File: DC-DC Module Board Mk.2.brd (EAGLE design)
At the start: 177.9 x 101.7 mm, 148 parts, among them U1 PCA9685, U3 LM1085IS-5.0

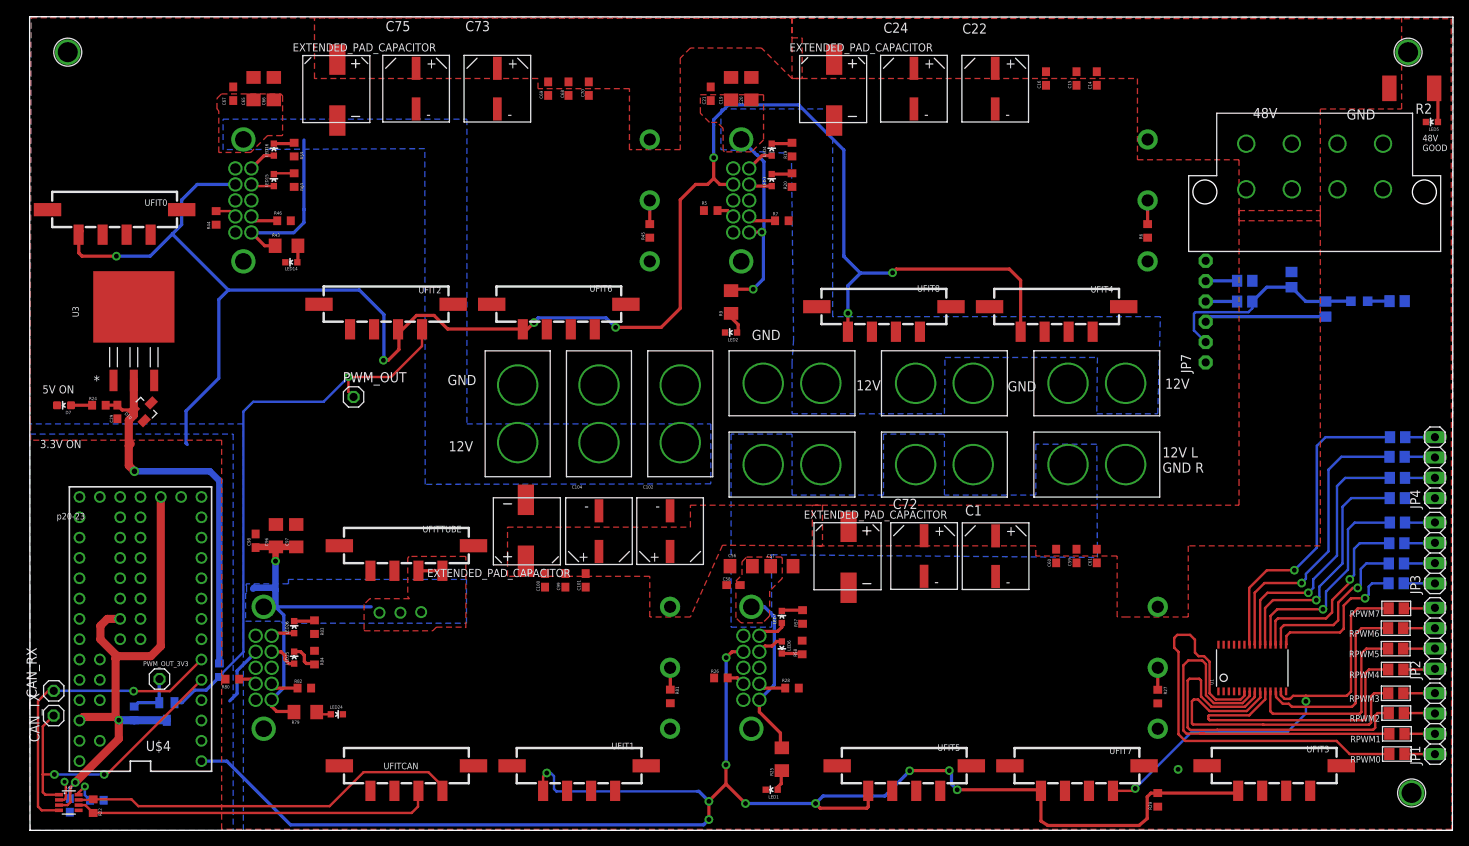
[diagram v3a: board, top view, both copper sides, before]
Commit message: Added and Reworked Traces
Added Traces mostly to the PWN and rerouted and cleaned up some other
traces
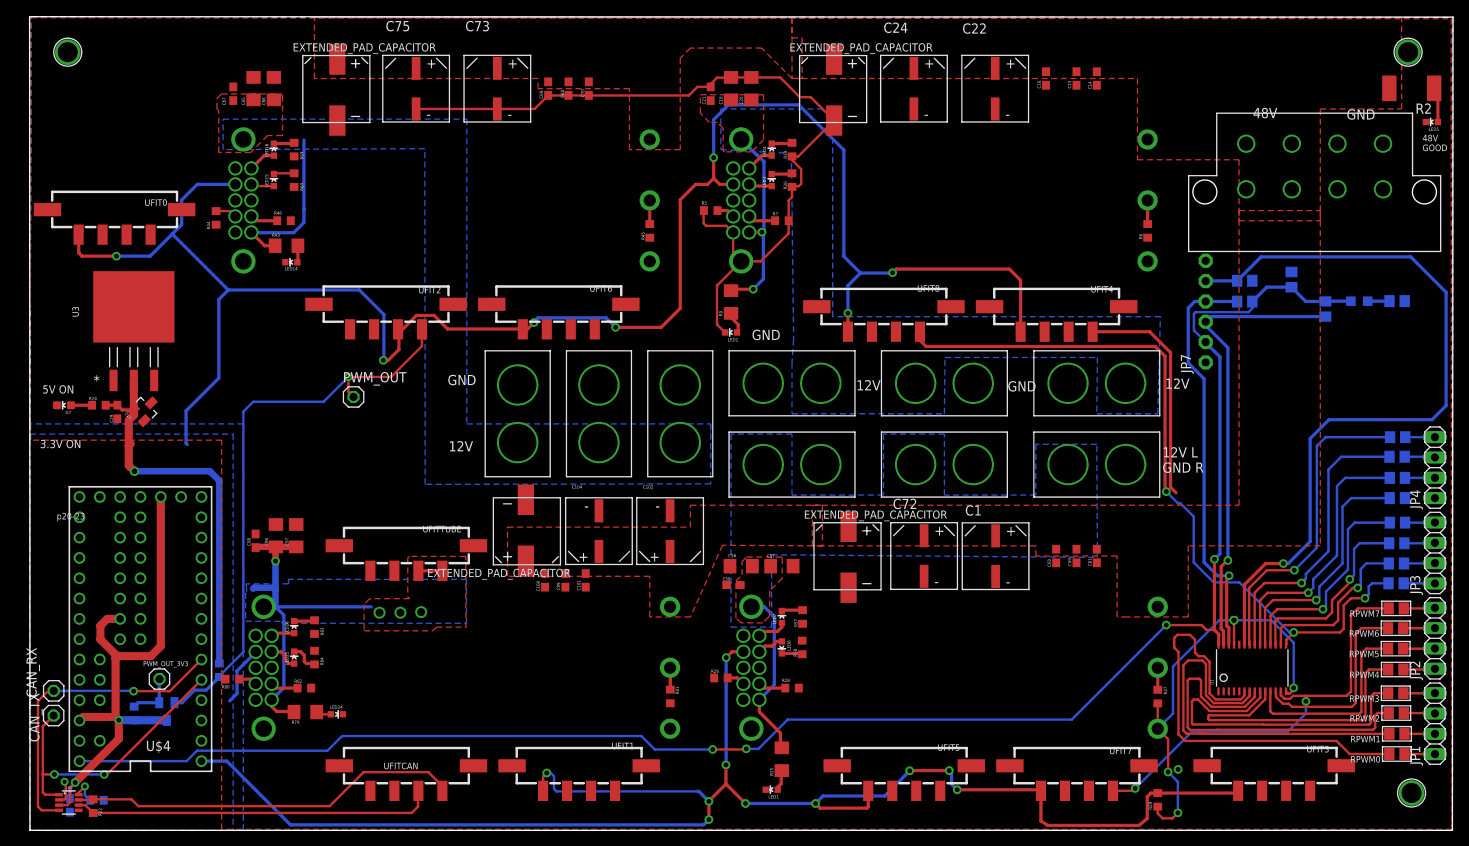
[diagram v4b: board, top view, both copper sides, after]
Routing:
- net VCC: track 26.4 -> 216.0 mm, vias 0 -> 4
- net GND: track 0.00 -> 158.5 mm, vias 0 -> 5
- net OE: track 3.97 -> 96.9 mm, vias 0 -> 1
- net PWM8: track 18.9 -> 94.7 mm, vias 1 -> 3
- net SCL: track 3.94 -> 51.7 mm, vias 0 -> 1
- net SDA: track 15.2 -> 57.3 mm, vias 0 -> 1
- net PWM4: track 37.8 -> 66.4 mm

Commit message: fixed a few DRC issues, added vias for pwm chans
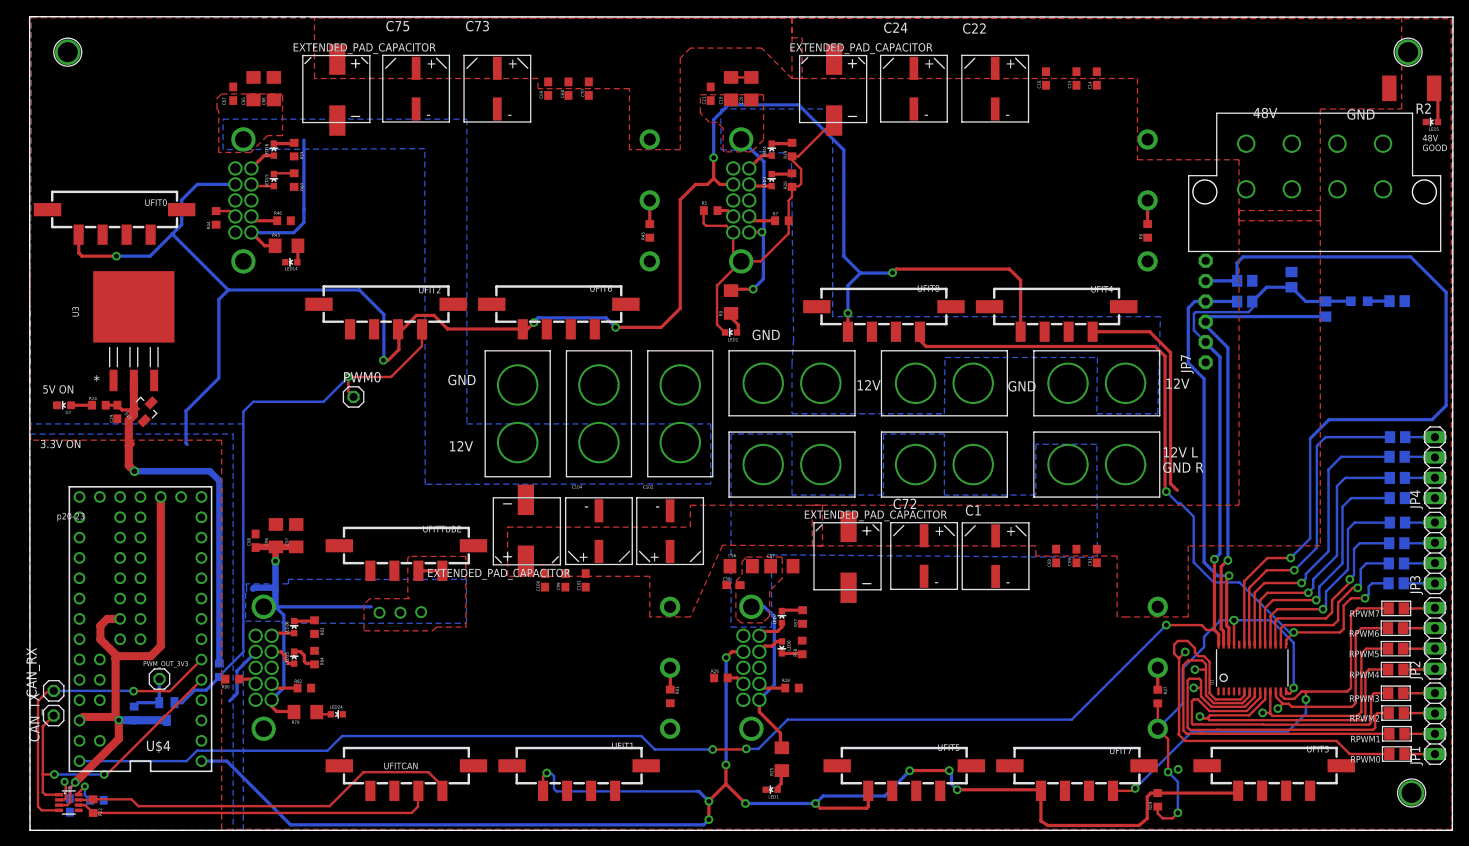
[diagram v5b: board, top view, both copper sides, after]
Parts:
- renumbered PWM_OUT to PWM0
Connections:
- removed net PWM_OUT: PWM0.1, R18.1, U$12.2, UFIT2.C4
- net PWM0: now also PWM0.1, R18.1, U$12.2, UFIT2.C4
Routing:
- net PWM_OUT: track 71.9 -> 0.00 mm, vias 1 -> 0
- net PWM0: track 55.9 -> 127.3 mm, vias 0 -> 2
- net GND: track 158.5 -> 105.1 mm
- net PWM5: track 25.0 -> 26.4 mm, vias 0 -> 1
- net OE: track 96.9 -> 98.2 mm
- net PWM1: track 48.6 -> 49.9 mm, vias 0 -> 1
- net PWM2: track 45.2 -> 46.1 mm, vias 0 -> 1
- net PWM6: track 24.3 -> 25.2 mm, vias 0 -> 1
- net PWM4: track 66.4 -> 67.3 mm, vias 0 -> 1
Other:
- board text added: "is this an attempt to bridge GND planes?"
- board text added: "possible GND islands"

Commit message: finished tracing, fixed bugs, added info, moved sparrow
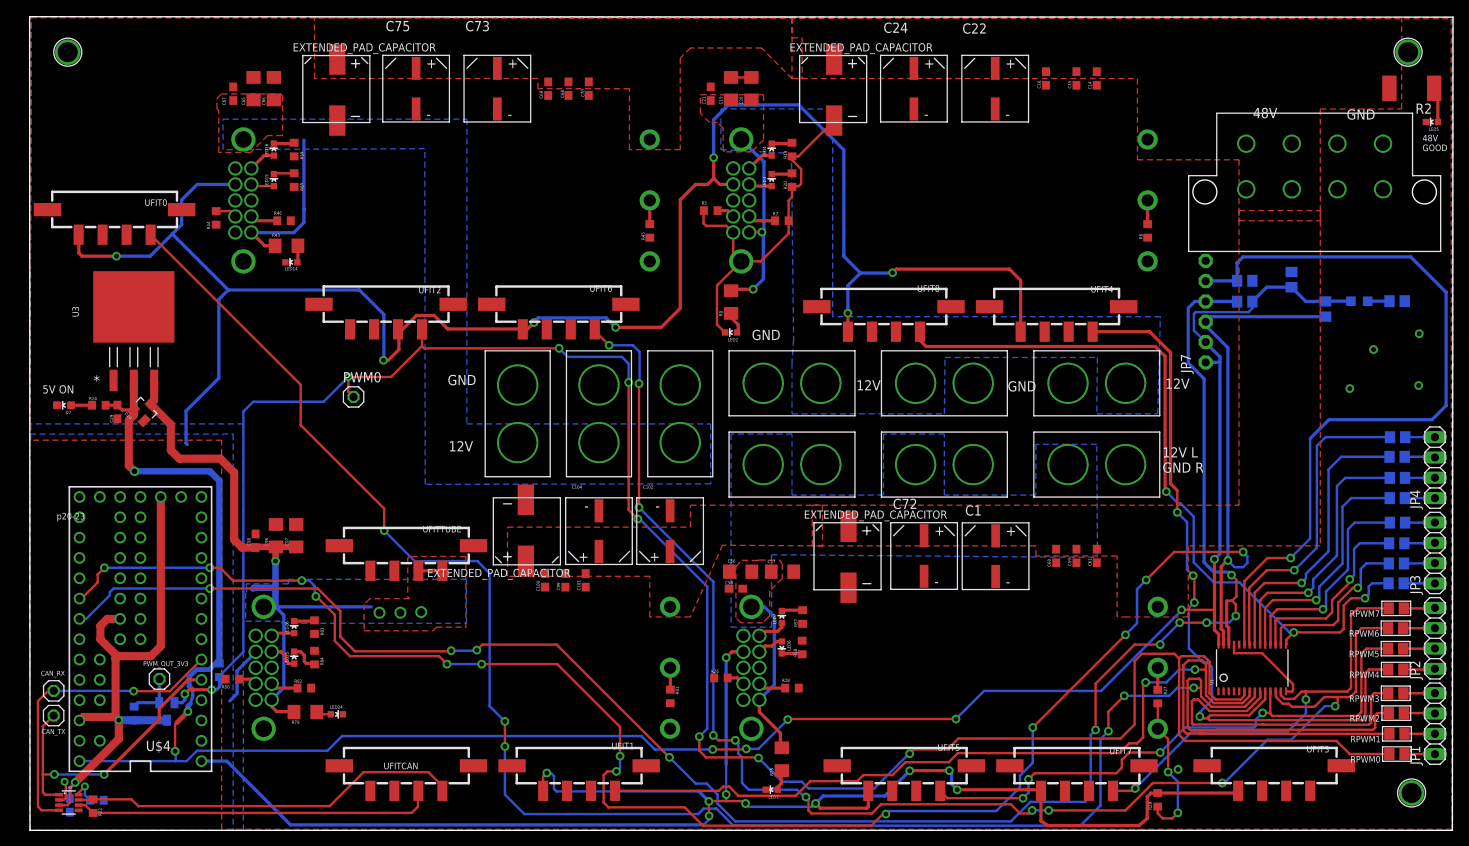
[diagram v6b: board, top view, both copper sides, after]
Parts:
- moved C56 0.69 mm to (88.8, 31.1)
- moved C57 0.69 mm to (94.1, 31.1)
- moved C58 0.55 mm to (88.2, 28.9)
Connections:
- removed net 5.0V: JP7.1
- removed net VCC: C3.1, JP7.2, LED8.A, R34.2, R35.2, U$4.VIN, U1.28
- net +5V: now also C3.1, JP7.1, JP7.2, LED8.A, R34.2, R35.2, U$4.VIN, U1.28
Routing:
- net +5V: track 50.0 -> 284.1 mm, vias 1 -> 9
- net VCC: track 216.0 -> 0.00 mm, vias 4 -> 0
- net SDA: track 57.3 -> 254.6 mm, vias 1 -> 14
- net PWM2: track 46.1 -> 240.8 mm, vias 1 -> 6
- net SCL: track 51.7 -> 235.6 mm, vias 1 -> 10
- net PWM6: track 25.2 -> 175.2 mm, vias 1 -> 10
- net PWM0: track 127.3 -> 277.2 mm, vias 2 -> 9
- net PWM1: track 49.9 -> 133.5 mm, vias 1 -> 2
- net PWM5: track 26.4 -> 73.5 mm, vias 1 -> 4
- net PWM4: track 67.3 -> 98.8 mm, vias 1 -> 4
- net +12V4: track 48.6 -> 79.1 mm
- net GND: track 105.1 -> 79.4 mm, vias 5 -> 2
- net N$38: track 0.00 -> 3.75 mm
- net TXD: track 37.0 -> 38.1 mm
- net DGND: track 442.0 -> 442.7 mm
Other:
- board text added: "DC-DC Module Verson: 2.1 Carolyn Lewelling, Alan Han, Nick Loffredo, Bayley Clausen 2016.05.01"
- board text added: "GND vias"
- board text removed: "3.3V ON"
- board text removed: "ADD INFO HERE YAY"
- board text removed: "is this an attempt to bridge GND planes?"
- board text removed: "possible GND islands"

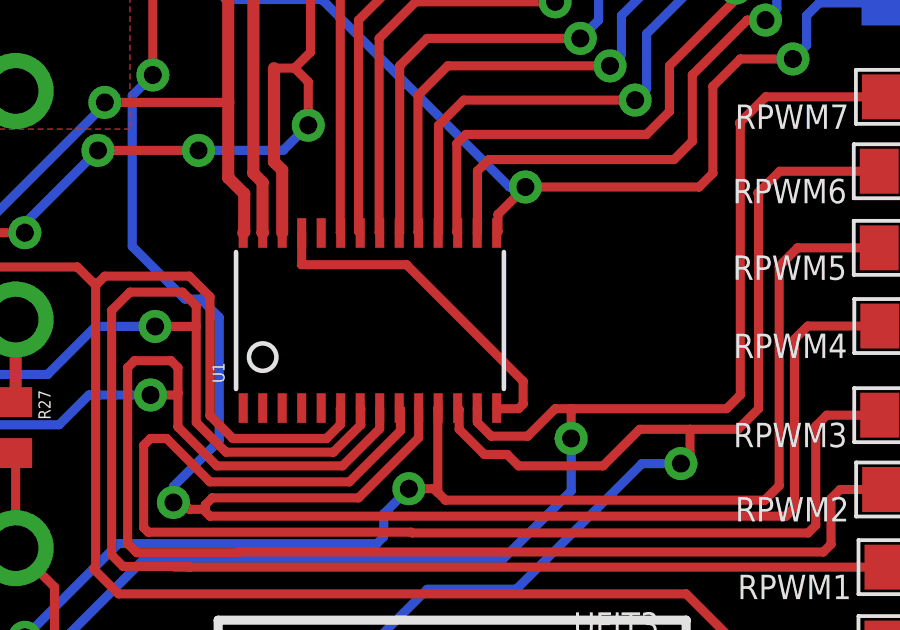
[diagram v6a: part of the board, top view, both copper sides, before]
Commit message: fixed GND vias
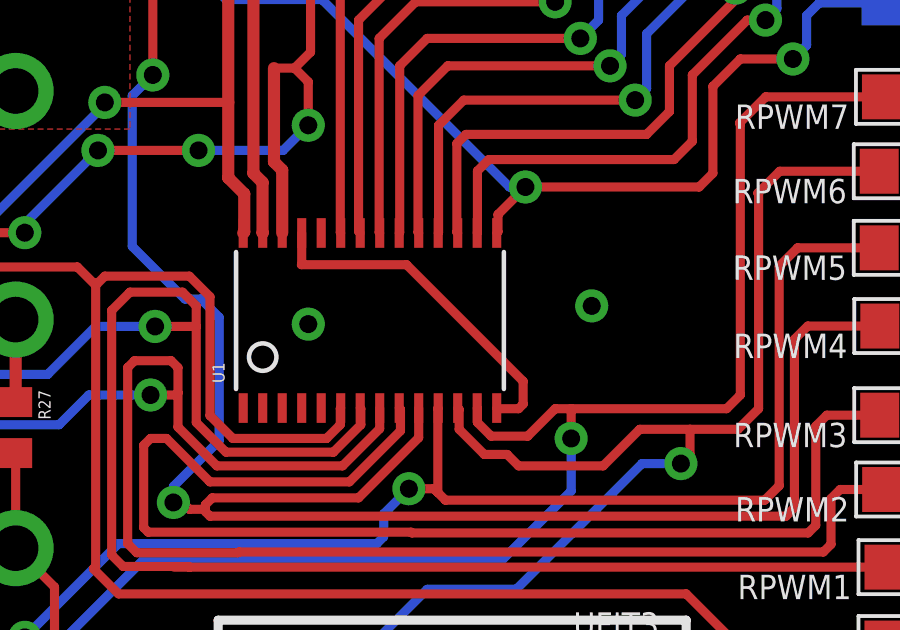
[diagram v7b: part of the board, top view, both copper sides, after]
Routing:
- net GND: vias 2 -> 8
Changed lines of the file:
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@@
 <wire x1="157.8864" y1="16.9926" x2="157.8864" y2="16.2306" width="0.3048" layer="1"/>
 <wire x1="157.8864" y1="16.2306" x2="157.734" y2="16.0782" width="0.3048" layer="1"/>
+<via x="164.973" y="53.9496" extent="1-16" drill="0.6"/>
+<via x="167.9448" y="58.8264" extent="1-16" drill="0.6"/>
+<via x="173.6598" y="60.8076" extent="1-16" drill="0.6"/>
+<via x="173.5836" y="54.3306" extent="1-16" drill="0.6"/>
+<via x="160.1724" y="19.5072" extent="1-16" drill="0.6"/>
+<via x="150.7236" y="18.8976" extent="1-16" drill="0.6"/>
 </signal>
 <signal name="N$7">
@@
 <contactref element="UFIT3" pad="C4"/>
 </signal>
-<signal name="N$5">
-<via x="173.6598" y="60.8076" extent="1-16" drill="0.6"/>
-</signal>
-<signal name="N$47">
-<via x="164.973" y="53.9496" extent="1-16" drill="0.6"/>
-</signal>
-<signal name="N$48">
-<via x="167.9448" y="58.8264" extent="1-16" drill="0.6"/>
-</signal>
-<signal name="N$49">
-<via x="173.5836" y="54.3306" extent="1-16" drill="0.6"/>
-</signal>
 </signals>
